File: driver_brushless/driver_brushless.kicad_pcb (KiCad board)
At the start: 2 copper layers, 37 parts, among them U1 B_Plug_5mm, U5 L6235D

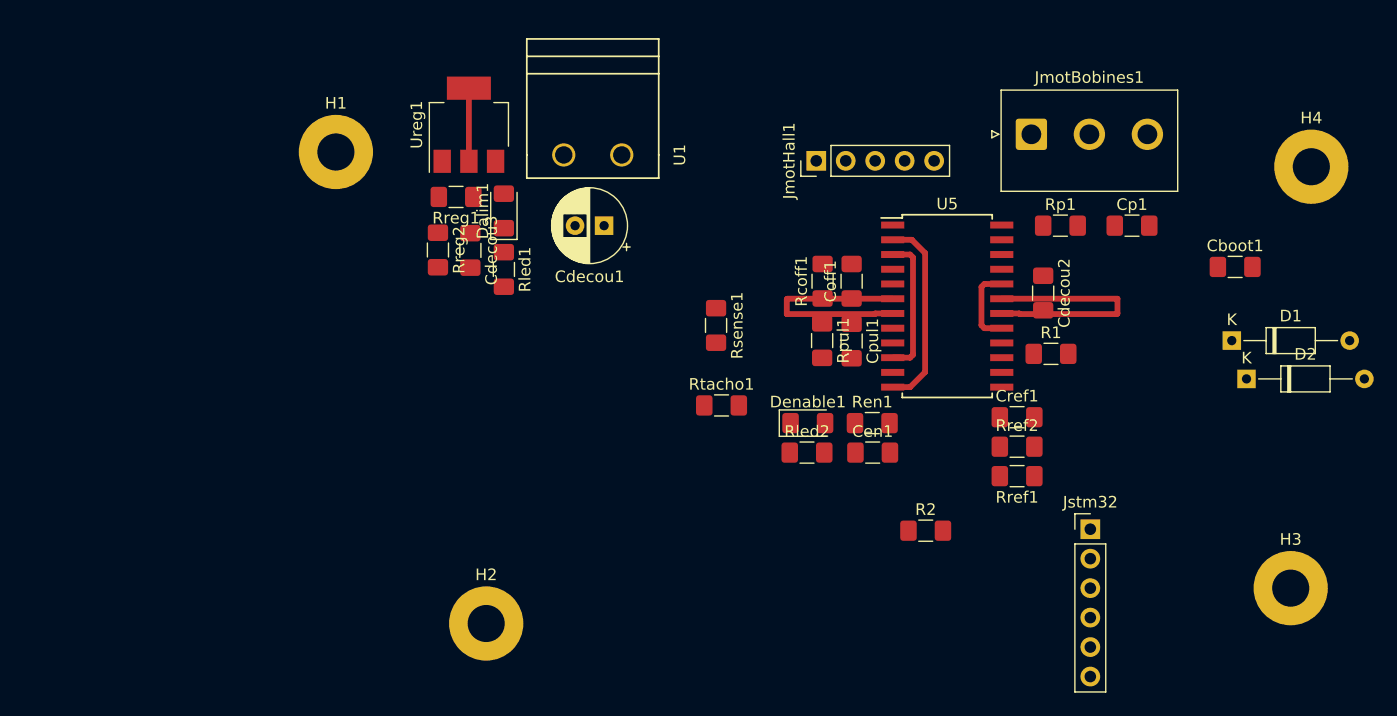
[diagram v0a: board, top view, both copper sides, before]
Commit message: modif driver moteur
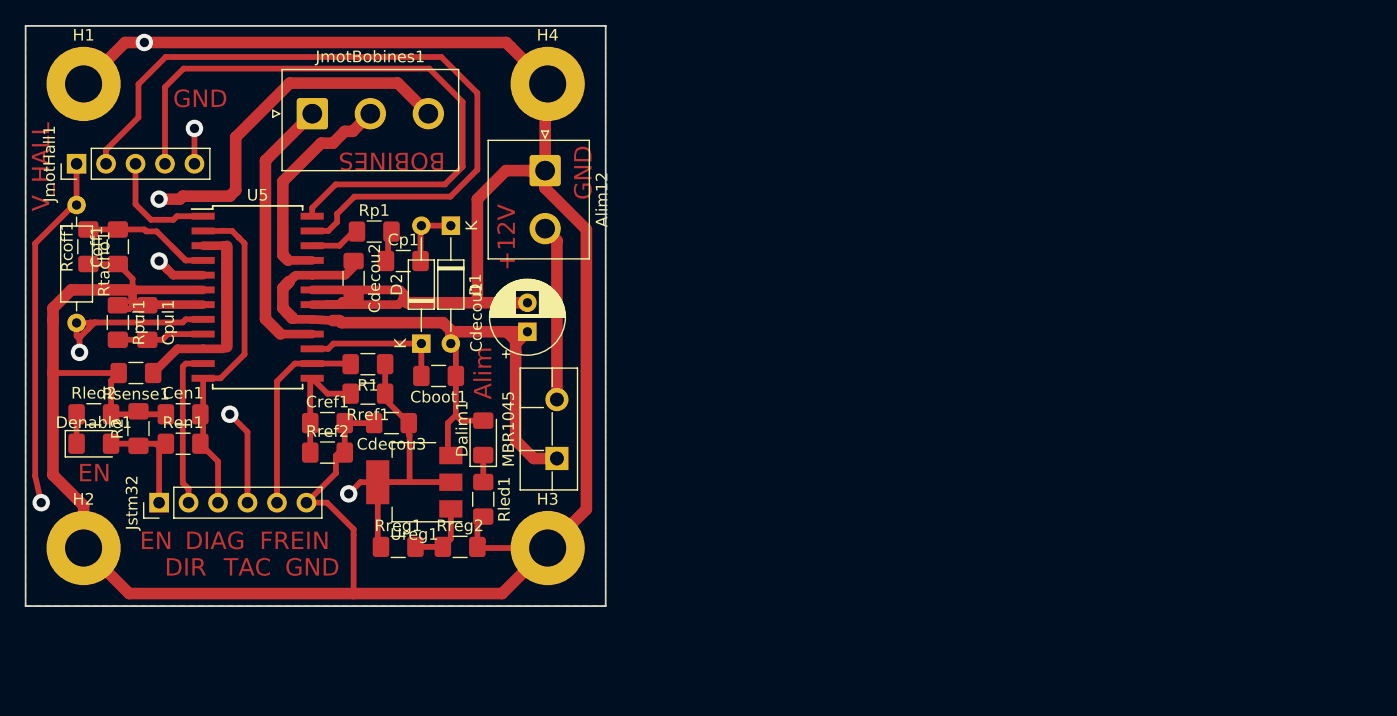
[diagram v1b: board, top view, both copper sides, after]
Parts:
- removed U1: B_Plug_5mm, B plug:Bplug-5mm
- added Alim12: B_Plug_5mm, Connector_JST:JST_NV_B02P-NV_1x02_P5.00mm_Vertical, F.Cu at (144.8, 72.5)
- added MBR1045: D_Schottky, Package_TO_SOT_THT:TO-220F-2_Vertical, F.Cu at (145.8, 97.3)
- Rtacho1: footprint Resistor_SMD:R_1206_3216Metric_Pad1.42x1.75mm_HandSolder -> Resistor_THT:R_Axial_DIN0207_L6.3mm_D2.5mm_P10.16mm_Horizontal
- moved Jstm32 80.3 mm to (111.5, 101.1), turned to 90 degrees
- moved D2 71.2 mm to (134.1, 87.4), turned to 90 degrees
- moved Cboot1 69.3 mm to (135.6, 90.2), turned to 180 degrees
- moved R2 68.4 mm to (109.7, 94.7), turned to 90 degrees
- moved D1 68.0 mm to (136.7, 77.2), turned to 270 degrees
- moved H4 66.2 mm to (145.0, 65.0)
- moved H3 64.1 mm to (145.0, 105.0)
- moved JmotHall1 63.8 mm to (104.4, 71.9)
- moved Rcoff1 63.4 mm to (105.4, 79.0)
- moved Coff1 63.3 mm to (108.0, 79.0)
- moved Cp1 62.9 mm to (132.6, 80.3)
- moved JmotBobines1 62.0 mm to (124.7, 67.6)
- moved Denable1 61.6 mm to (105.9, 96.0)
- moved Rled2 61.6 mm to (105.9, 93.5)
- moved Cpul1 60.7 mm to (110.5, 85.6)
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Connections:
- JmotBobines1 pad 1: /Out_11 -> /Out_31
- JmotBobines1 pad 3: /Out_31 -> /Out_11
- Jstm32 pad 1: Net-(Cen1-Pad2) -> Net-(Denable1-Pad2)
- Jstm32 pad 2: Net-(Denable1-Pad2) -> Net-(Jstm32-Pad2)
- Jstm32 pad 3: Net-(Jstm32-Pad3) -> Net-(Cen1-Pad2)
- R1 pad 2: Net-(Jstm32-Pad4) -> Net-(Jstm32-Pad5)
- Rtacho1 pad 2: Net-(Jstm32-Pad5) -> Net-(Jstm32-Pad4)
- U5 pad 11: Net-(Jstm32-Pad3) -> Net-(Jstm32-Pad2)
- U5 pad 14: Net-(Jstm32-Pad4) -> Net-(Jstm32-Pad5)
- U5 pad 8: Net-(Jstm32-Pad5) -> Net-(Jstm32-Pad4)
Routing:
- net GND: track 40.8 -> 276.6 mm, vias 0 -> 2
- net /Hall_sensor_21: track 0.00 -> 62.9 mm
- net +12V: track 7.02 -> 63.2 mm
- net /Hall_sensor_31: track 0.00 -> 54.9 mm
- net +5V: track 6.30 -> 56.7 mm, vias 0 -> 2
- net /Out_11: track 0.00 -> 37.6 mm, vias 0 -> 2
- net /Out_31: track 0.00 -> 23.9 mm
- net Net-(Jstm32-Pad4): track 0.00 -> 23.8 mm, vias 0 -> 2
- net /Out_21: track 0.00 -> 19.0 mm
- net Net-(Jstm32-Pad5): track 0.00 -> 17.5 mm
- net Net-(Alim12-Pad2): track 0.00 -> 15.2 mm
- net Net-(Jstm32-Pad2): track 0.00 -> 13.8 mm
- net Net-(Coff1-Pad2): track 0.00 -> 12.7 mm
- net Net-(Cen1-Pad2): track 18.3 -> 30.9 mm
- net Net-(Cboot1-Pad2): track 0.00 -> 12.4 mm
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- added copper zone on F.Cu, net GND
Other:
- board outline added: 50 x 50 mm
- net class Default: via_dia 0.8 -> 1.5; via_drill 0.4 -> 0.8
- board text added: "+12V"
- board text added: "Alim"
- board text added: "BOBINES"
- board text added: "DIAG"
- board text added: "DIR"
- board text added: "EN"
- board text added: "FREIN"
- board text added: "GND"
- board text added: "TAC"
- board text added: "V_HALL"

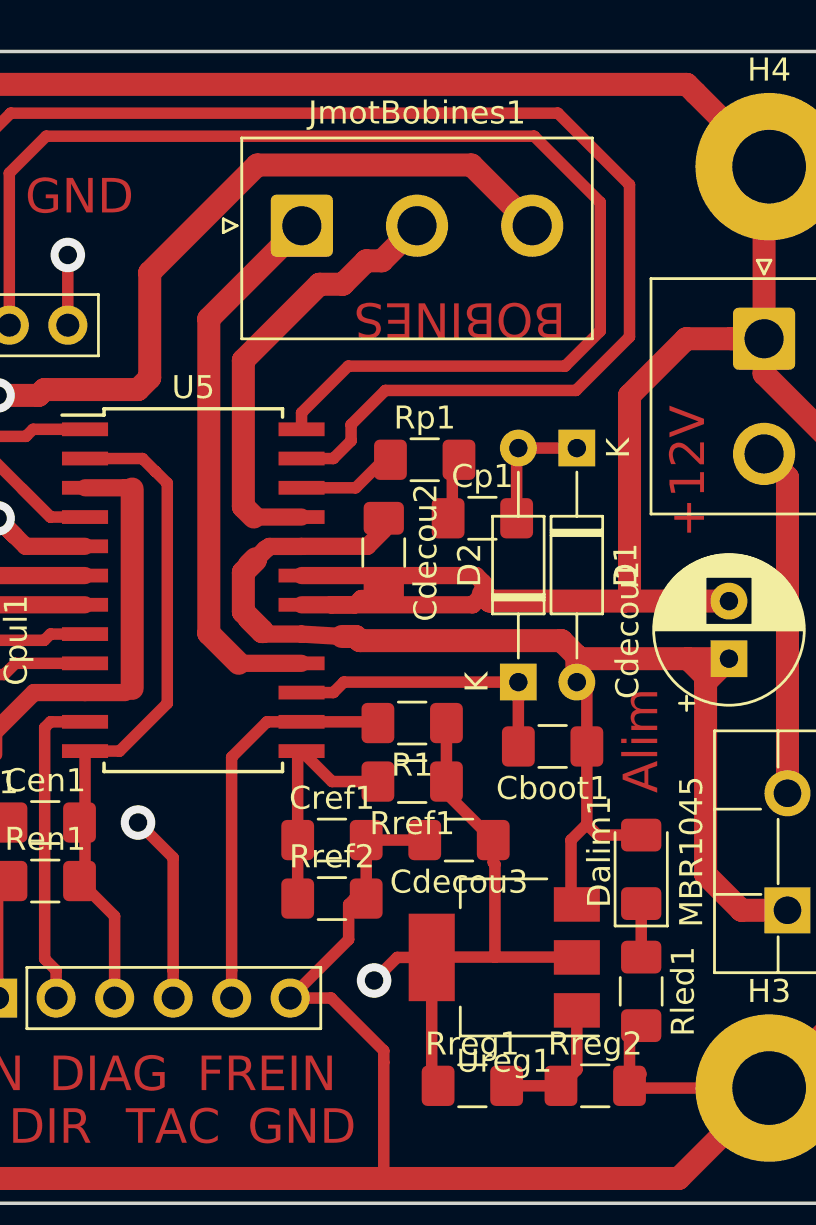
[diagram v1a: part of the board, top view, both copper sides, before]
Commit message: modif driver moteur
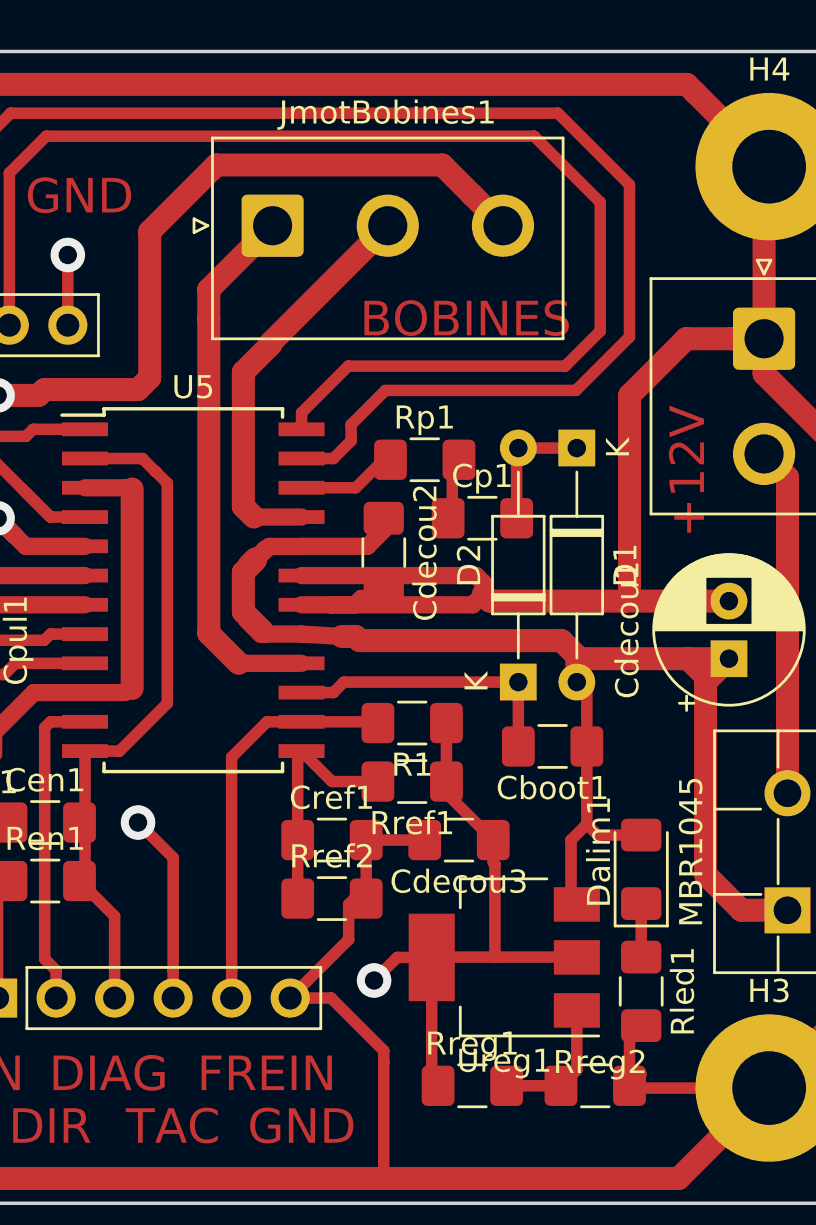
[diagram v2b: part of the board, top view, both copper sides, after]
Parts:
- moved JmotBobines1 1.27 mm to (123.4, 67.6)
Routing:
- net /Out_21: track 19.0 -> 17.5 mm
- net /Out_31: track 23.9 -> 23.4 mm
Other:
- board text removed: "Alim"
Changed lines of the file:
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@@
   (general
     (thickness 1.6)
-    (drawings 17)
-    (tracks 285)
+    (drawings 16)
+    (tracks 286)
     (zones 0)
     (modules 38)
@@
   )
   (setup
-    (last_trace_width 1)
+    (last_trace_width 0.5)
     (user_trace_width 0.75)
     (user_trace_width 1)
@@
   )
   (module Connector_JST:JST_NV_B03P-NV_1x03_P5.00mm_Vertical (layer F.Cu)
-    (at 124.714 67.564)
+    (at 123.444 67.564)
     (descr "JST NV series connector, B03P-NV (http://www.jst-mfg.com/product/pdf/eng/eNV.pdf), generated with kicad-footprint-generator")
     (tags "connector JST NV side entry")
@@
     (tags "resistor handsolder")
     (attr smd)
-    (fp_text reference Rreg2 (at 0 -1.82) (layer F.SilkS)
+    (fp_text reference Rreg2 (at 0.2175 -1.016) (layer F.SilkS)
       (effects (font (size 1 1) (thickness 0.15)))
     )
@@
     )
   )
-  (gr_text BOBINES (at 131.572 71.628 180) (layer F.Cu)
+  (gr_text BOBINES (at 131.826 71.628) (layer F.Cu)
     (effects (font (size 1.5 1.5) (thickness 0.3)))
   )
   (gr_text EN (at 105.918 98.552) (layer F.Cu)
-    (effects (font (size 1.5 1.5) (thickness 0.3)))
-  )
-  (gr_text Alim (at 139.446 89.916 90) (layer F.Cu)
     (effects (font (size 1.5 1.5) (thickness 0.3)))
   )
@@
   (segment (start 111.506 80.264) (end 112.268 81.026) (width 0.75) (layer F.Cu) (net 14))
   (via (at 111.506 80.264) (size 1.5) (drill 0.8) (layers F.Cu B.Cu) (net 14))
-  (segment (start 132.078009 64.928009) (end 134.714 67.564) (width 1) (layer F.Cu) (net 14))
   (segment (start 113.284 74.93) (end 113.538 74.676) (width 1) (layer F.Cu) (net 14))
   (segment (start 111.506 74.93) (end 113.284 74.93) (width 1) (layer F.Cu) (net 14))
+  (segment (start 113.538 74.676) (end 117.602 74.676) (width 1) (layer F.Cu) (net 14))
+  (segment (start 118.11 74.168) (end 118.11 67.818) (width 1) (layer F.Cu) (net 14))
   (segment (start 117.602 74.676) (end 118.11 74.168) (width 1) (layer F.Cu) (net 14))
-  (segment (start 122.777991 64.928009) (end 132.078009 64.928009) (width 1) (layer F.Cu) (net 14))
-  (segment (start 118.11 74.168) (end 118.11 69.596) (width 1) (layer F.Cu) (net 14))
-  (segment (start 113.538 74.676) (end 117.602 74.676) (width 1) (layer F.Cu) (net 14))
-  (segment (start 118.11 69.596) (end 122.777991 64.928009) (width 1) (layer F.Cu) (net 14))
+  (segment (start 118.11 67.818) (end 120.999991 64.928009) (width 1) (layer F.Cu) (net 14))
+  (segment (start 132.094001 66.21201) (end 130.81 64.928009) (width 1) (layer F.Cu) (net 14))
+  (segment (start 132.094001 66.214001) (end 132.094001 66.21201) (width 1) (layer F.Cu) (net 14))
+  (segment (start 133.444 67.564) (end 132.094001 66.214001) (width 1) (layer F.Cu) (net 14))
+  (segment (start 120.999991 64.928009) (end 130.81 64.928009) (width 1) (layer F.Cu) (net 14))
   (segment (start 122.629001 80.211001) (end 124.701001 80.211001) (width 0.75) (layer F.Cu) (net 15))
-  (segment (start 128.19 69.088) (end 127.508 69.088) (width 1) (layer F.Cu) (net 15))
-  (segment (start 127.508 69.088) (end 126.492 70.104) (width 1) (layer F.Cu) (net 15))
   (segment (start 122.174 79.756) (end 122.629001 80.211001) (width 1) (layer F.Cu) (net 15))
-  (segment (start 129.714 67.564) (end 128.19 69.088) (width 1) (layer F.Cu) (net 15))
-  (segment (start 125.476 70.104) (end 122.174 73.406) (width 1) (layer F.Cu) (net 15))
-  (segment (start 126.492 70.104) (end 125.476 70.104) (width 1) (layer F.Cu) (net 15))
-  (segment (start 122.174 73.406) (end 122.174 79.756) (width 1) (layer F.Cu) (net 15))
+  (segment (start 123.364 72.724) (end 122.174 73.914) (width 1) (layer F.Cu) (net 15))
+  (segment (start 123.364 72.644) (end 128.444 67.564) (width 1) (layer F.Cu) (net 15))
+  (segment (start 123.364 72.644) (end 123.364 72.724) (width 1) (layer F.Cu) (net 15))
+  (segment (start 122.174 73.914) (end 122.174 79.756) (width 1) (layer F.Cu) (net 15))
   (segment (start 124.701001 86.561001) (end 121.972999 86.561001) (width 0.75) (layer F.Cu) (net 16))
   (segment (start 120.67399 85.261992) (end 121.972999 86.561001) (width 1) (layer F.Cu) (net 16))
-  (segment (start 124.714 67.564) (end 120.67399 71.60401) (width 1) (layer F.Cu) (net 16))
   (segment (start 120.67399 71.60401) (end 120.67399 85.261992) (width 1) (layer F.Cu) (net 16))
+  (segment (start 120.67399 70.33401) (end 123.444 67.564) (width 1) (layer F.Cu) (net 16))
+  (segment (start 120.67399 71.60401) (end 120.67399 70.33401) (width 1) (layer F.Cu) (net 16))
   (segment (start 106.934 70.679919) (end 106.934 71.882) (width 0.5) (layer F.Cu) (net 17))
   (segment (start 109.728 65.024) (end 109.728 67.885919) (width 0.5) (layer F.Cu) (net 17))
   (segment (start 112.074011 62.677989) (end 109.728 65.024) (width 0.5) (layer F.Cu) (net 17))
   (segment (start 135.829989 62.677989) (end 112.074011 62.677989) (width 0.5) (layer F.Cu) (net 17))
-  (segment (start 138.938 65.786) (end 135.829989 62.677989) (width 0.5) (layer F.Cu) (net 17))
   (segment (start 109.728 67.885919) (end 106.934 70.679919) (width 0.5) (layer F.Cu) (net 17))
-  (segment (start 138.938 72.39) (end 138.938 65.786) (width 0.5) (layer F.Cu) (net 17))
   (segment (start 126.851494 76.90051) (end 126.851494 76.2) (width 0.5) (layer F.Cu) (net 17))
   (segment (start 124.701001 77.671001) (end 126.081003 77.671001) (width 0.5) (layer F.Cu) (net 17))
-  (segment (start 136.61373 74.71427) (end 138.938 72.39) (width 0.5) (layer F.Cu) (net 17))
   (segment (start 126.081003 77.671001) (end 126.851494 76.90051) (width 0.5) (layer F.Cu) (net 17))
   (segment (start 126.851494 76.2) (end 128.337224 74.71427) (width 0.5) (layer F.Cu) (net 17))
   (segment (start 128.337224 74.71427) (end 136.61373 74.71427) (width 0.5) (layer F.Cu) (net 17))
+  (segment (start 136.61373 74.71427) (end 138.938 72.39) (width 0.5) (layer F.Cu) (net 17))
+  (segment (start 138.938 65.786) (end 135.829989 62.677989) (width 0.5) (layer F.Cu) (net 17))
+  (segment (start 138.938 72.39) (end 138.938 65.786) (width 0.5) (layer F.Cu) (net 17))
   (segment (start 113.042999 76.401001) (end 115.301001 76.401001) (width 0.5) (layer F.Cu) (net 18))
   (segment (start 112.736 76.708) (end 113.042999 76.401001) (width 0.5) (layer F.Cu) (net 18))
@@
   (segment (start 124.701001 75.685001) (end 126.726002 73.66) (width 0.5) (layer F.Cu) (net 19))
   (segment (start 126.726002 73.66) (end 136.144 73.66) (width 0.5) (layer F.Cu) (net 19))
+  (segment (start 124.701001 76.401001) (end 124.701001 75.685001) (width 0.5) (layer F.Cu) (net 19))
   (segment (start 136.144 73.66) (end 137.668 72.136) (width 0.5) (layer F.Cu) (net 19))
-  (segment (start 124.701001 76.401001) (end 124.701001 75.685001) (width 0.5) (layer F.Cu) (net 19))
   (segment (start 137.668 66.548) (end 134.797999 63.677999) (width 0.5) (layer F.Cu) (net 19))
   (segment (start 137.668 72.136) (end 137.668 66.548) (width 0.5) (layer F.Cu) (net 19))

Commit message: driver brushless
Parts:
- Cdecou1: footprint Capacitor_THT:CP_Radial_D6.3mm_P2.50mm -> Capacitor_THT:CP_Radial_D8.0mm_P5.00mm
- Rled2: value 330 -> 680
- moved Cdecou1 1.77 mm to (142.2, 87.8)
- moved MBR1045 0.76 mm to (145.8, 98.0)
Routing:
- net +12V: track 63.2 -> 58.5 mm
- net Net-(Alim12-Pad2): track 15.2 -> 17.4 mm
- net GND: track 276.6 -> 275.3 mm
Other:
- board text added: "Alim"
